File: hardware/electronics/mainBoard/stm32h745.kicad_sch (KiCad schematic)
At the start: 65 parts, among them SW1 PTS810, SW2 PTS810, U1 STM32H745ZIT6, U2 TCAN3403-Q1

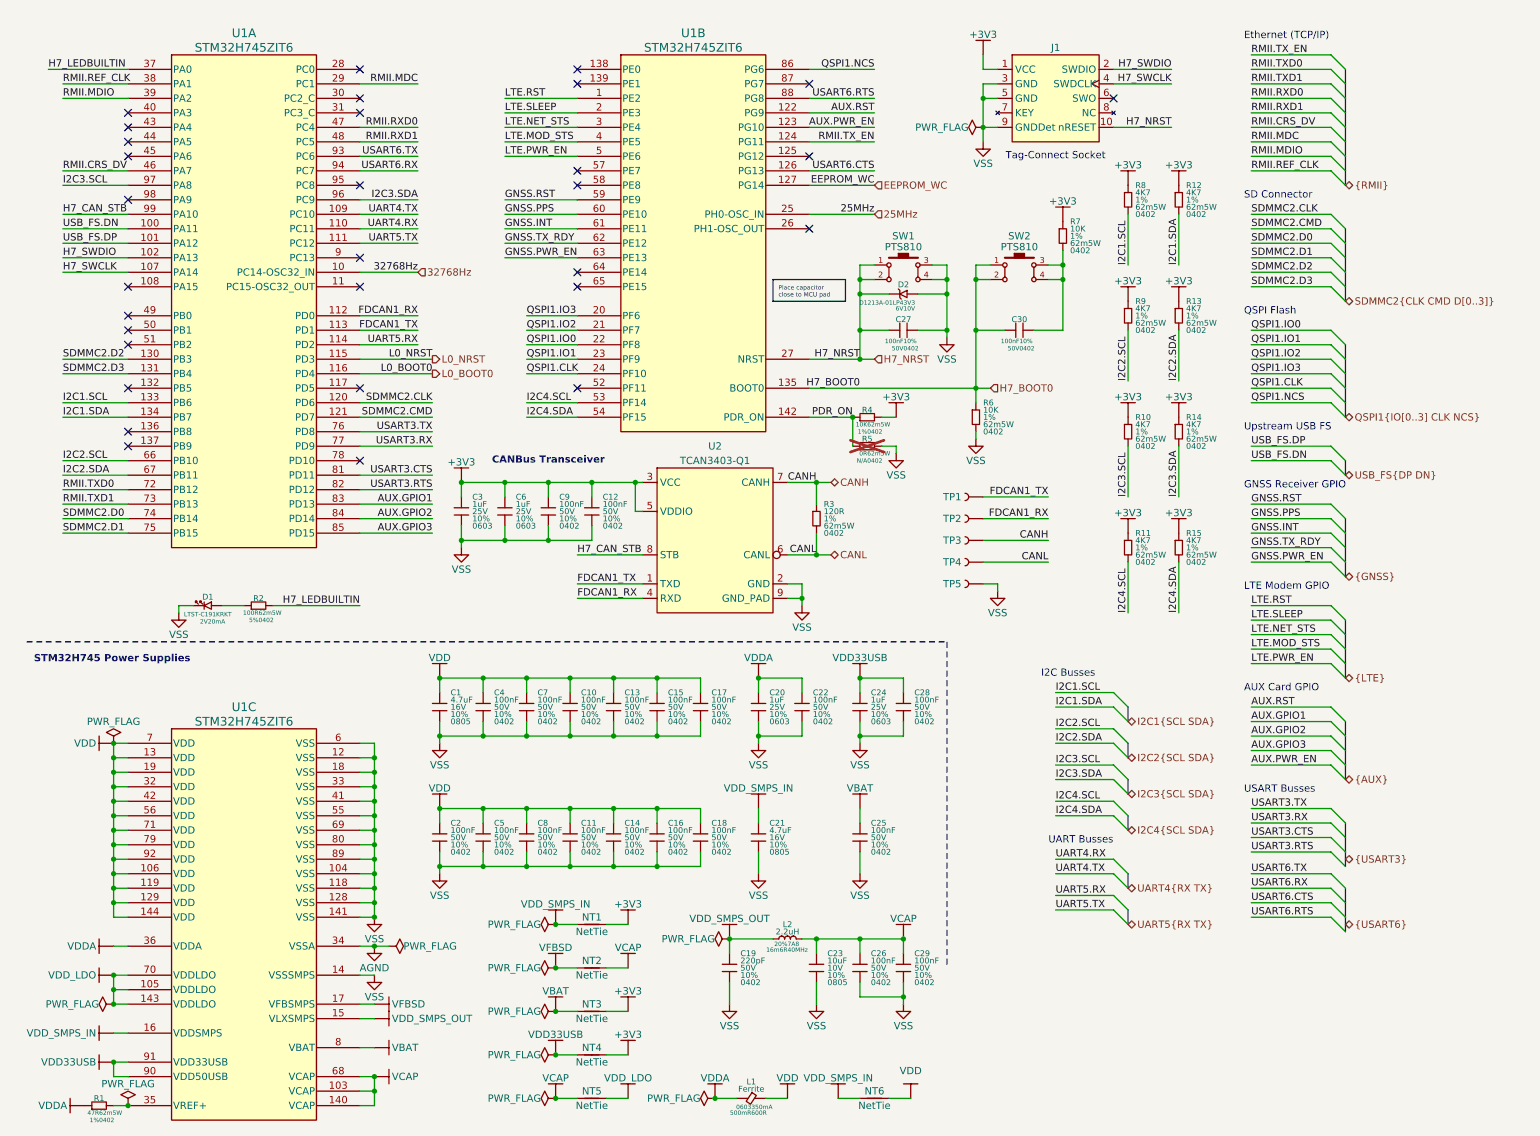
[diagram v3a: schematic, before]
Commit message: moved CAN transceivers to their own page
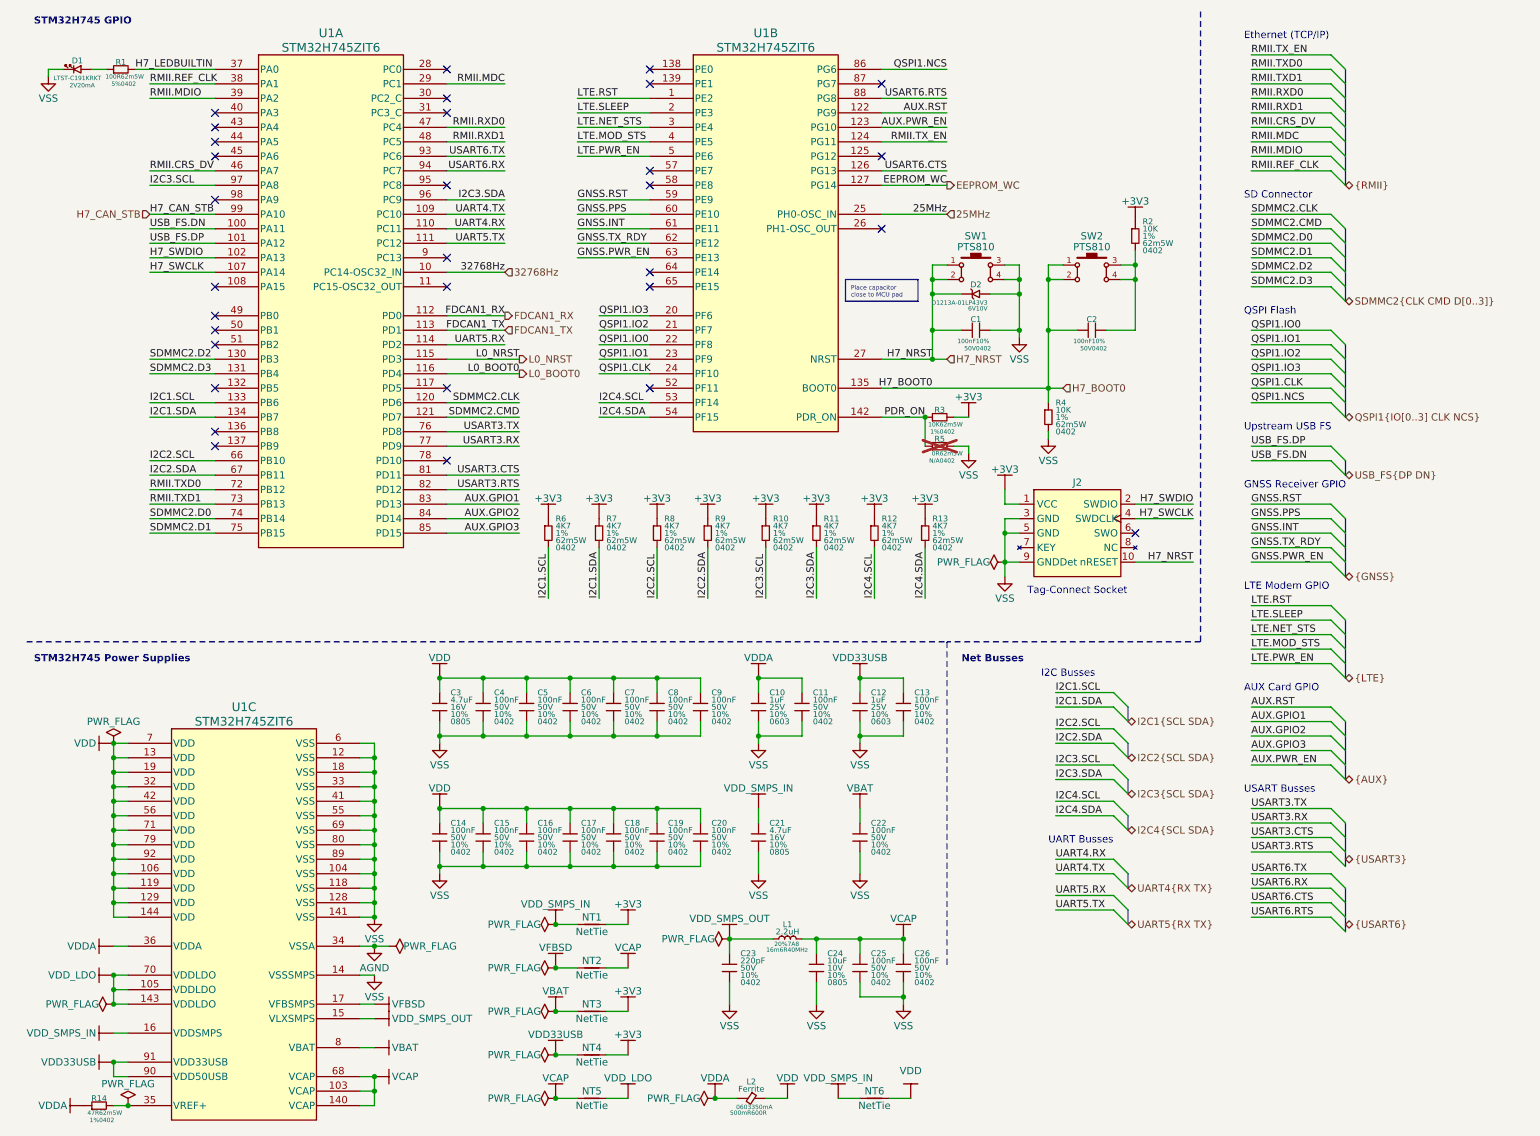
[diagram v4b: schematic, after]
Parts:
- removed C12, C9: 100nF, symbol lib_sch:C
- removed C3, C6: 1uF, symbol lib_sch:C
- removed R3: 120R, symbol lib_sch:R
- removed TP1, TP2, TP3, TP4: ~, symbol lib_sch:Testpoint
- removed TP5: RCWCTE, symbol lib_sch:Testpoint
- removed U2: TCAN3403-Q1, symbol lib_sch:TCAN340x-Q1
- renumbered C27 to C1, C20 to C10, C22 to C11, C24 to C12, C28 to C13, C2 to C14, C5 to C15, C8 to C16, C11 to C17, C14 to C18, C16 to C19, C30 to C2, C18 to C20, C25 to C22, C19 to C23, C23 to C24, C26 to C25, C29 to C26, C1 to C3, C7 to C5, C10 to C6, C13 to C7, C15 to C8, C17 to C9, J1 to J2, L2 to L1, L1 to L2, R2 to R1, R14 to R11, R11 to R12, R15 to R13, R1 to R14, R7 to R2, R4 to R3, R6 to R4, R8 to R6, R12 to R7, R9 to R8, R13 to R9
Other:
- note added: "Net Busses"
- note added: "STM32H745 GPIO"
- note removed: "CANBus Transceiver"
- moved on the sheet: C1, C2, D1, D2, J2, R1, R10, R11, R12, R13, R2, R3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

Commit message: assigned FPs
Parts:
- D2: footprint (none) -> lib_diodes:XDFN2P65_100X60X50L50X25L
- SW1, SW2: footprint (none) -> lib_switches:PTS810
- U1: footprint (none) -> lib_ICs:LQFP-144
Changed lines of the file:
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@@
 			)
 		)
-		(property "Footprint" ""
+		(property "Footprint" "lib_ICs:LQFP-144"
 			(at 139.446 50.8 0)
 			(effects
@@
 			)
 		)
-		(property "Footprint" ""
+		(property "Footprint" "lib_ICs:LQFP-144"
 			(at 48.006 170.18 0)
 			(effects
@@
 			)
 		)
-		(property "Footprint" ""
+		(property "Footprint" "lib_ICs:LQFP-144"
 			(at 63.246 60.96 0)
 			(effects
@@
 			)
 		)
-		(property "Footprint" ""
+		(property "Footprint" "lib_switches:PTS810"
 			(at 187.325 55.88 0)
 			(effects
@@
 			)
 		)
-		(property "Footprint" ""
+		(property "Footprint" "lib_diodes:XDFN2P65_100X60X50L50X25L"
 			(at 177.165 59.055 0)
 			(effects
@@
 			)
 		)
-		(property "Footprint" ""
+		(property "Footprint" "lib_switches:PTS810"
 			(at 207.645 55.88 0)
 			(effects

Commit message: added footprints to symbols
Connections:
- net H7_NRST: now also D2.1; no longer D2.2
- net VSS: now also D2.2; no longer D2.1

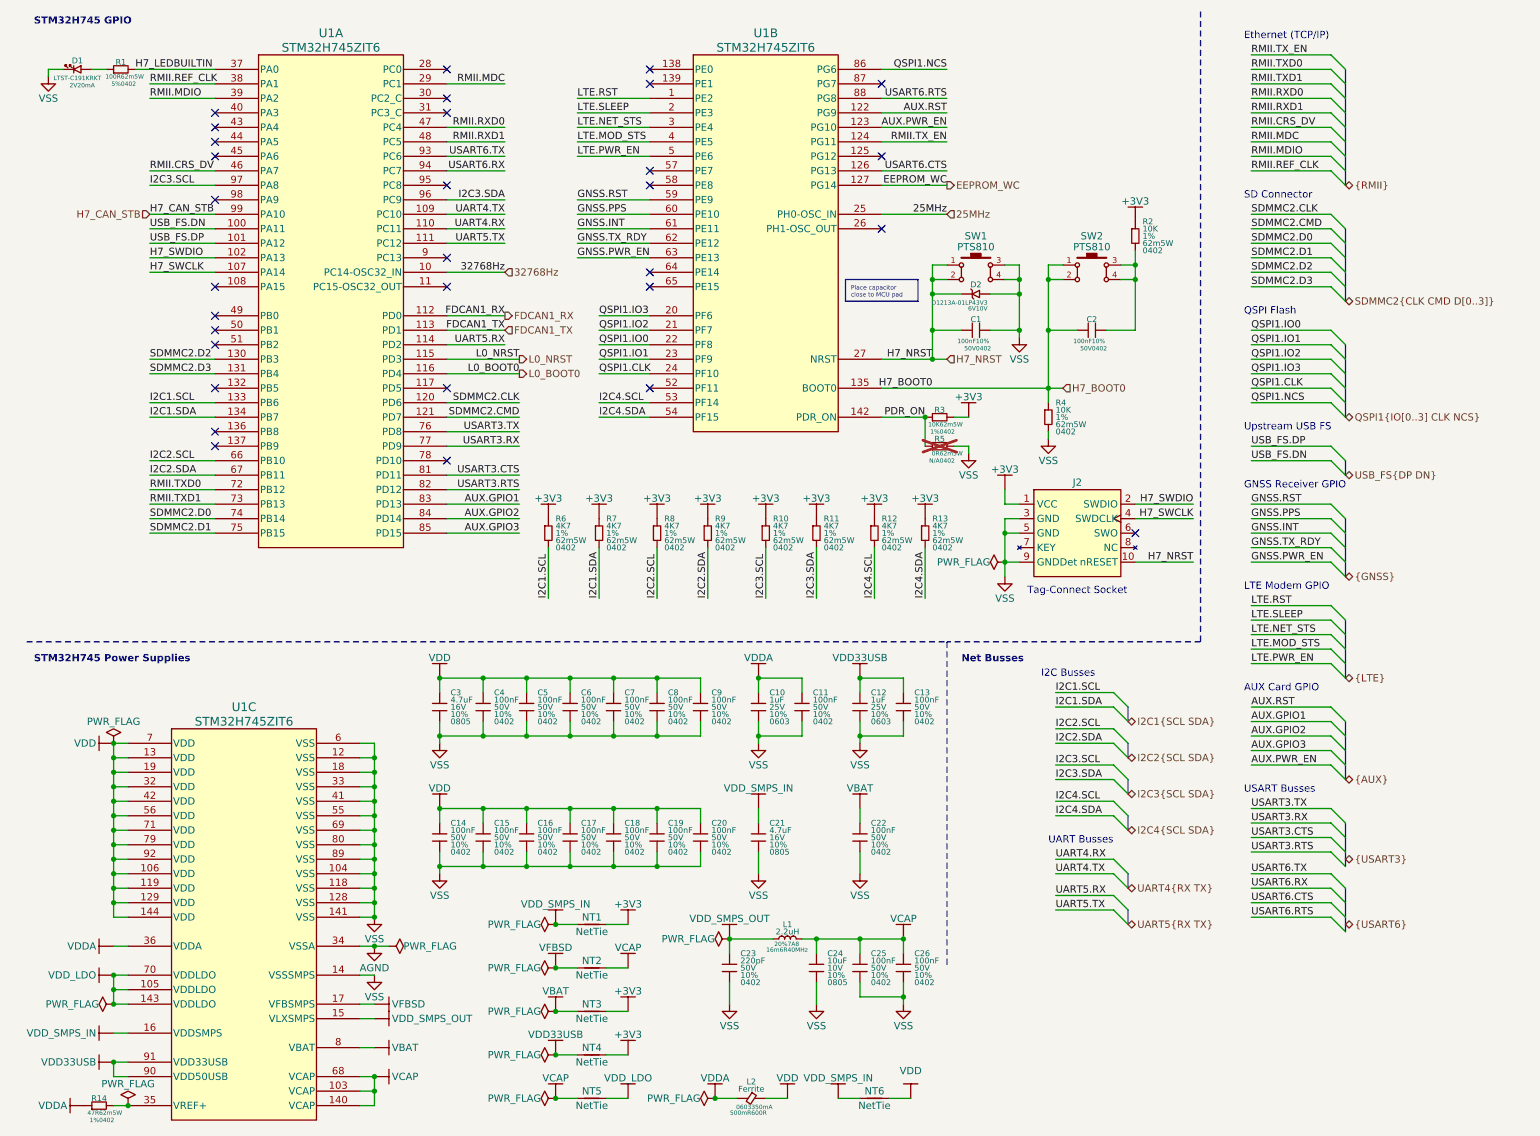
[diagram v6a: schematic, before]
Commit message: assigned footprints
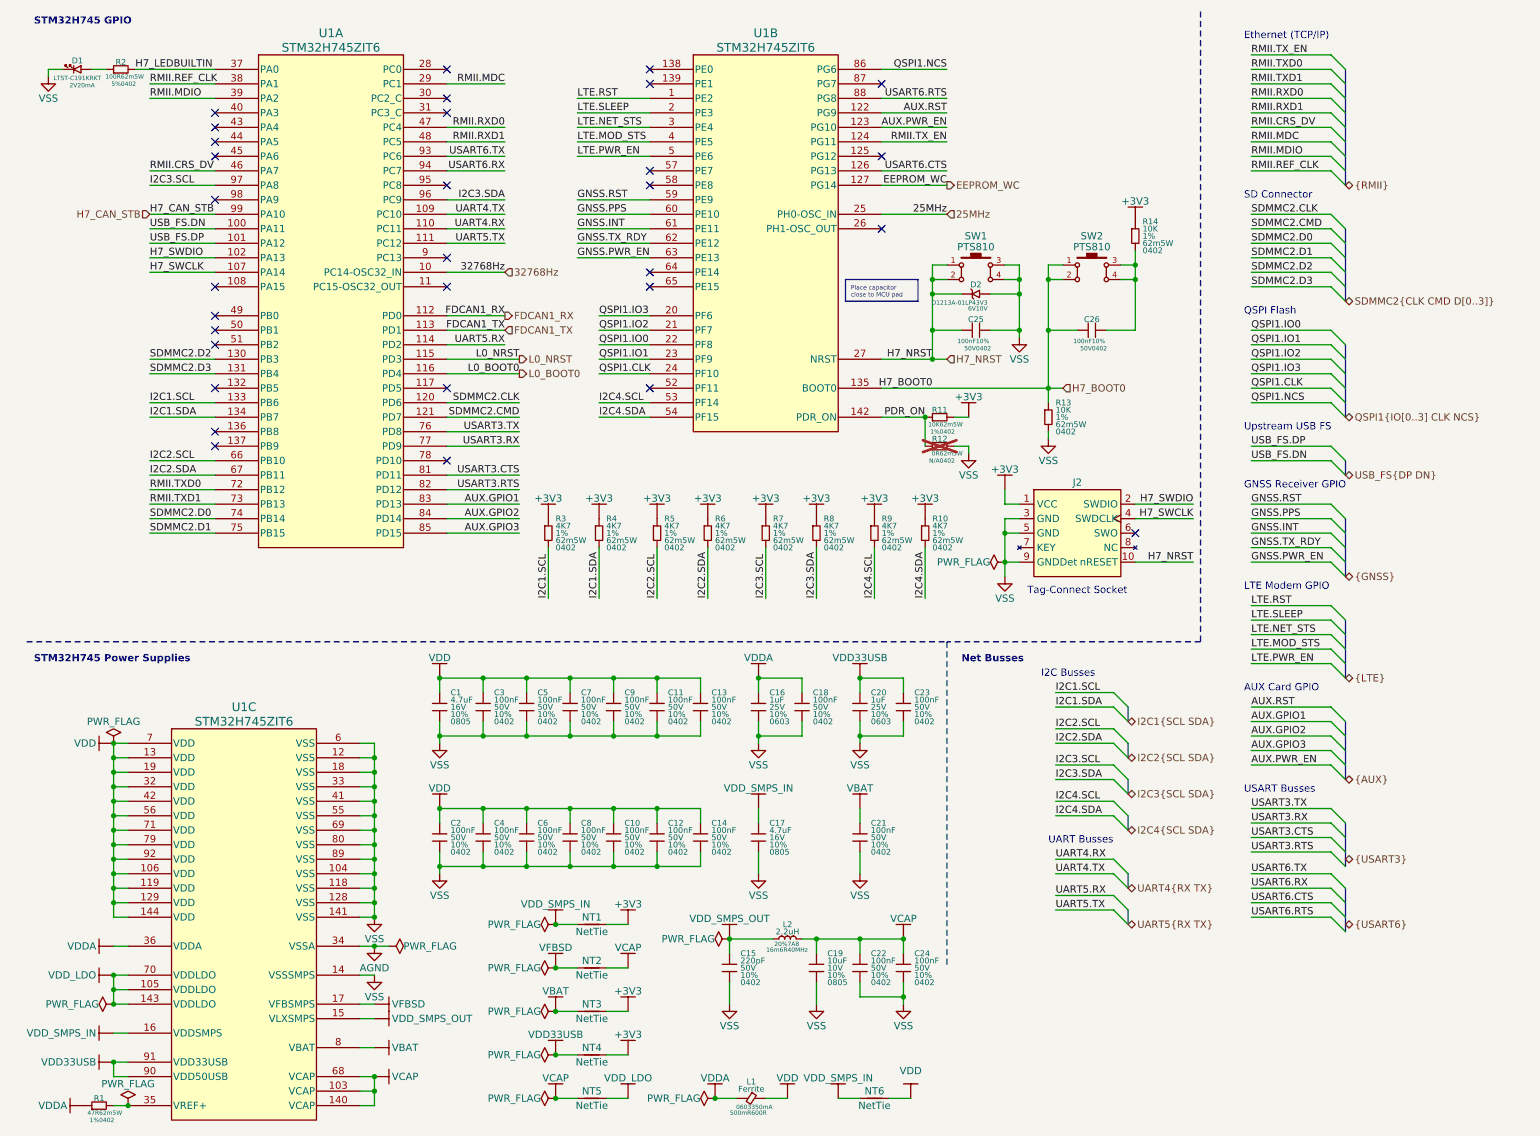
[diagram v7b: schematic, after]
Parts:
- C1: renamed from C3; footprint (none) -> lib_passives:GCM0805
- C10: renamed from C18; footprint (none) -> lib_passives:GCM0402
- C11: renamed from C8; footprint (none) -> lib_passives:GCM0402
- C12: renamed from C19; footprint (none) -> lib_passives:GCM0402
- C13: renamed from C9; footprint (none) -> lib_passives:GCM0402
- C14: renamed from C20; footprint (none) -> lib_passives:GCM0402
- C15: renamed from C23; footprint (none) -> lib_passives:GCM0402
- C16: renamed from C10; footprint (none) -> lib_passives:GRT0603
- C17: renamed from C21; footprint (none) -> lib_passives:GCM0805
- C18: renamed from C11; footprint (none) -> lib_passives:GCM0402
- C19: renamed from C24; footprint (none) -> lib_passives:GCM0805
- C2: renamed from C14; footprint (none) -> lib_passives:GCM0402
- C20: renamed from C12; footprint (none) -> lib_passives:GRT0603
- C21: renamed from C22; footprint (none) -> lib_passives:GCM0402
- C22: renamed from C25; footprint (none) -> lib_passives:GCM0402
- C23: renamed from C13; footprint (none) -> lib_passives:GCM0402
- C24: renamed from C26; footprint (none) -> lib_passives:GCM0402
- C25: renamed from C1; footprint (none) -> lib_passives:GCM0402
- C26: renamed from C2; footprint (none) -> lib_passives:GCM0402
- C3: renamed from C4; footprint (none) -> lib_passives:GCM0402
- C4: renamed from C15; footprint (none) -> lib_passives:GCM0402
- C5: footprint (none) -> lib_passives:GCM0402
- C6: renamed from C16; footprint (none) -> lib_passives:GCM0402
- C7: renamed from C6; footprint (none) -> lib_passives:GCM0402
- C8: renamed from C17; footprint (none) -> lib_passives:GCM0402
- C9: renamed from C7; footprint (none) -> lib_passives:GCM0402
- D1: footprint (none) -> lib_diodes:LTST-0603
- J2: footprint (none) -> lib_misc:TC2050-FP
- L1: renamed from L2; footprint (none) -> lib_passives:L_0603
- L2: renamed from L1; footprint (none) -> lib_passives:WE-XHMI-4030
- NT1, NT2, NT3, NT4, NT5, NT6: footprint (none) -> lib_misc:NetTie-2_SMD_Pad2.0mm
- R1: renamed from R14; footprint (none) -> lib_passives:CRCW0402
- R10: renamed from R13; footprint (none) -> lib_passives:CRCW0402
- R11: renamed from R3; footprint (none) -> lib_passives:CRCW0402
- R12: renamed from R5; footprint (none) -> lib_passives:CRCW0402
- R13: renamed from R4; footprint (none) -> lib_passives:CRCW0402
- R14: renamed from R2; footprint (none) -> lib_passives:CRCW0402
- R2: renamed from R1; footprint (none) -> lib_passives:CRCW0402
- R3: renamed from R6; footprint (none) -> lib_passives:CRCW0402
- R4: renamed from R7; footprint (none) -> lib_passives:CRCW0402
- R5: renamed from R8; footprint (none) -> lib_passives:CRCW0402
- R6: renamed from R9; footprint (none) -> lib_passives:CRCW0402
- R7: renamed from R10; footprint (none) -> lib_passives:CRCW0402
- R8: renamed from R11; footprint (none) -> lib_passives:CRCW0402
- R9: renamed from R12; footprint (none) -> lib_passives:CRCW0402

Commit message: assigned net classes
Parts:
- renumbered C25 to C1, C16 to C10, C18 to C11, C20 to C12, C23 to C13, C2 to C14, C4 to C15, C6 to C16, C8 to C17, C10 to C18, C12 to C19, C26 to C2, C14 to C20, C17 to C21, C21 to C22, C15 to C23, C19 to C24, C22 to C25, C24 to C26, C1 to C3, C3 to C4, C7 to C6, C9 to C7, C11 to C8, C13 to C9, L2 to L1, L1 to L2, R2 to R1, R7 to R10, R8 to R11, R9 to R12, R10 to R13, R1 to R14, R14 to R2, R11 to R3, R13 to R4, R12 to R5, R3 to R6, R4 to R7, R5 to R8, R6 to R9
